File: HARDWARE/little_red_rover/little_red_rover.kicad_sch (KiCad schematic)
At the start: 60 parts, among them J1 USB_C_Receptacle_USB2.0_14P, J2 Conn_01x04_Socket, J3 Conn_01x02_Socket, J4 Conn_01x02_Socket, J5 Conn_01x01_Socket, J6 Conn_01x01_Socket, J8 Conn_02x12_Odd_Even, SW1 SW_Push, SW2 SW_Push, SW3 SW_Push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

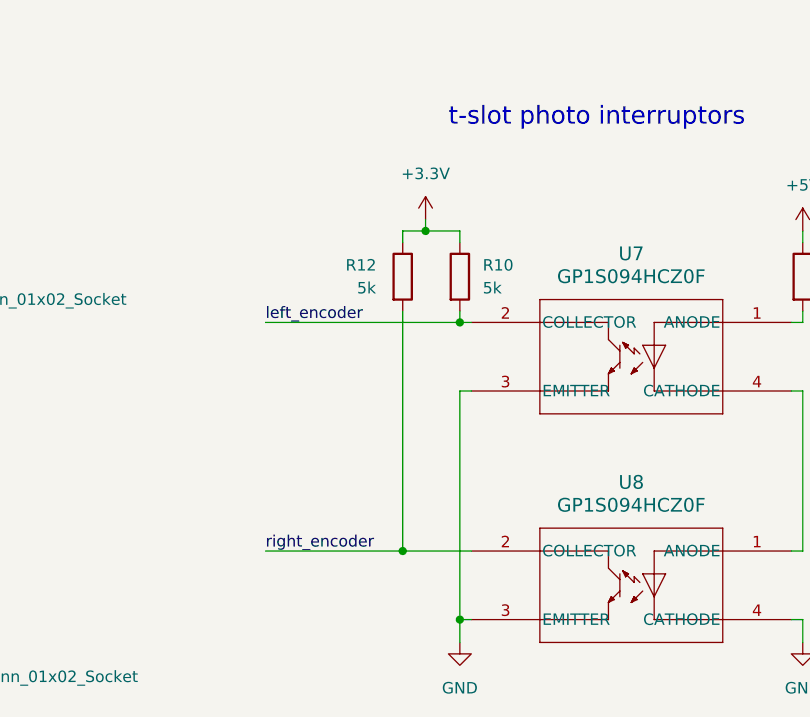
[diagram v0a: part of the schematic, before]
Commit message: Remove pull ups on photointerupters
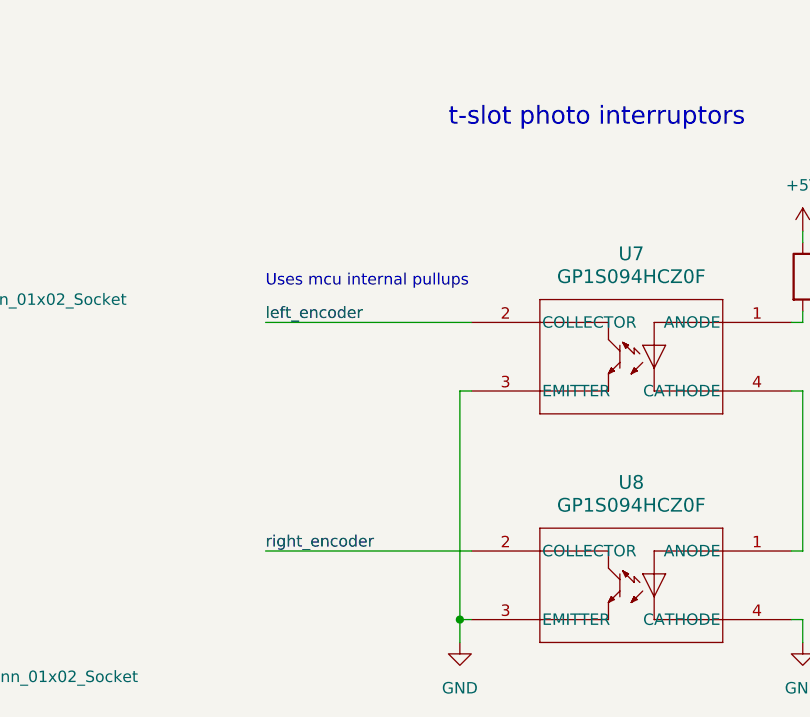
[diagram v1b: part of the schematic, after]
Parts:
- removed R10, R12: 5k, Resistor_SMD:R_0603_1608Metric_Pad0.98x0.95mm_HandSolder, symbol Device:R
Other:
- note added: "Uses mcu internal pullups"
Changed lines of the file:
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@@
   (junction (at 281.94 266.7) (diameter 0) (color 0 0 0 0)
   )
-  (junction (at 152.4 243.84) (diameter 0) (color 0 0 0 0)
-  )
   (junction (at 349.25 101.6) (diameter 0) (color 0 0 0 0)
   )
@@
   (junction (at 476.25 144.78) (diameter 0) (color 0 0 0 0)
   )
-  (junction (at 156.21 254) (diameter 0) (color 0 0 0 0)
-  )
   (junction (at 396.24 74.93) (diameter 0) (color 0 0 0 0)
   )
@@
   (junction (at 322.58 88.9) (diameter 0) (color 0 0 0 0)
   )
-  (junction (at 149.86 279.4) (diameter 0) (color 0 0 0 0)
-  )
   (junction (at 499.11 138.43) (diameter 0) (color 0 0 0 0)
   )
@@
     (stroke (width 0) (type default))
   )
-  (wire (pts (xy 149.86 279.4) (xy 157.48 279.4))
+  (wire (pts (xy 134.62 279.4) (xy 157.48 279.4))
     (stroke (width 0) (type default))
   )
@@
     (stroke (width 0) (type default))
   )
-  (wire (pts (xy 134.62 254) (xy 156.21 254))
-    (stroke (width 0) (type default))
-  )
   (wire (pts (xy 83.82 331.47) (xy 83.82 328.93))
     (stroke (width 0) (type default))
@@
     (stroke (width 0) (type default))
   )
-  (wire (pts (xy 149.86 245.11) (xy 149.86 243.84))
-    (stroke (width 0) (type default))
-  )
   (wire (pts (xy 46.99 73.66) (xy 67.31 73.66))
     (stroke (width 0) (type default))
@@
     (stroke (width 0) (type default))
   )
-  (wire (pts (xy 156.21 252.73) (xy 156.21 254))
-    (stroke (width 0) (type default))
-  )
   (wire (pts (xy 600.71 260.35) (xy 623.57 260.35))
     (stroke (width 0) (type default))
@@
     (stroke (width 0) (type default))
   )
-  (wire (pts (xy 152.4 242.57) (xy 152.4 243.84))
-    (stroke (width 0) (type default))
-  )
   (wire (pts (xy 57.15 342.9) (xy 68.58 342.9))
     (stroke (width 0) (type default))
@@
     (stroke (width 0) (type default))
   )
-  (wire (pts (xy 134.62 279.4) (xy 149.86 279.4))
-    (stroke (width 0) (type default))
-  )
   (wire (pts (xy 85.09 299.72) (xy 91.44 299.72))
     (stroke (width 0) (type default))
@@
     (stroke (width 0) (type default))
   )
-  (wire (pts (xy 149.86 252.73) (xy 149.86 279.4))
-    (stroke (width 0) (type default))
-  )
   (wire (pts (xy 392.43 158.75) (xy 392.43 161.29))
     (stroke (width 0) (type default))
@@
     (stroke (width 0) (type default))
   )
-  (wire (pts (xy 156.21 243.84) (xy 156.21 245.11))
-    (stroke (width 0) (type default))
-  )
   (wire (pts (xy 698.5 132.08) (xy 698.5 135.89))
     (stroke (width 0) (type default))
@@
     (stroke (width 0) (type default))
   )
-  (wire (pts (xy 156.21 243.84) (xy 152.4 243.84))
-    (stroke (width 0) (type default))
-  )
   (wire (pts (xy 322.58 73.66) (xy 328.93 73.66))
     (stroke (width 0) (type default))
@@
     (stroke (width 0) (type default))
   )
-  (wire (pts (xy 149.86 243.84) (xy 152.4 243.84))
-    (stroke (width 0) (type default))
-  )
   (wire (pts (xy 67.31 91.44) (xy 46.99 91.44))
     (stroke (width 0) (type default))
@@
     (stroke (width 0) (type default))
   )
-  (wire (pts (xy 156.21 254) (xy 157.48 254))
+  (wire (pts (xy 134.62 254) (xy 157.48 254))
     (stroke (width 0) (type default))
   )
@@
     (effects (font (size 5 5)) (justify left bottom))
   )
+  (text "Uses mcu internal pullups" (at 134.62 250.19 0)
+    (effects (font (size 1.27 1.27)) (justify left bottom))
+  )
   (text "headers" (at 628.65 35.56 0)
     (effects (font (size 5 5)) (justify left bottom))
@@
     )
   )
-  (symbol (lib_id "power:+3.3V") (at 152.4 242.57 0) (unit 1)
-    (in_bom yes) (on_board yes) (dnp no) (fields_autoplaced)
-    (property "Reference" "#PWR026" (at 152.4 246.38 0)
-      (effects (font (size 1.27 1.27)) hide)
-    )
-    (property "Value" "+3.3V" (at 152.4 237.49 0)
-      (effects (font (size 1.27 1.27)))
-    )
-    (property "Footprint" "" (at 152.4 242.57 0)
-      (effects (font (size 1.27 1.27)) hide)
-    )
-    (property "Datasheet" "" (at 152.4 242.57 0)
-      (effects (font (size 1.27 1.27)) hide)
-    )
-    (pin "1")
-    (instances
-      (project "little_red_rover"
-        (path "/6f482c50-19c8-43f6-b4b5-8739f6fb7866"
-          (reference "#PWR026") (unit 1)
-        )
-      )
-    )
-  )
   (symbol (lib_id "Device:R") (at 387.35 72.39 90) (unit 1)
     (in_bom yes) (on_board yes) (dnp no)
@@
     )
   )
-  (symbol (lib_id "Device:R") (at 149.86 248.92 0) (unit 1)
-    (in_bom yes) (on_board yes) (dnp no)
-    (property "Reference" "R12" (at 143.51 247.65 0)
-      (effects (font (size 1.27 1.27)) (justify left))
-    )
-    (property "Value" "5k" (at 144.78 250.19 0)
-      (effects (font (size 1.27 1.27)) (justify left))
-    )
-    (property "Footprint" "Resistor_SMD:R_0603_1608Metric_Pad0.98x0.95mm_HandSolder" (at 148.082 248.92 90)
-      (effects (font (size 1.27 1.27)) hide)
-    )
-    (property "Datasheet" "~" (at 149.86 248.92 0)
-      (effects (font (size 1.27 1.27)) hide)
-    )
-    (property "JLC" "0603" (at 149.86 248.92 0)
-      (effects (font (size 1.27 1.27)) hide)
-    )
-    (property "LCSC" "" (at 149.86 248.92 0)
-      (effects (font (size 1.27 1.27)) hide)
-    )
-    (pin "2")
-    (pin "1")
-    (instances
-      (project "little_red_rover"
-        (path "/6f482c50-19c8-43f6-b4b5-8739f6fb7866"
-          (reference "R12") (unit 1)
-        )
-      )
-    )
-  )
   (symbol (lib_id "power:GND") (at 623.57 280.67 0) (unit 1)
     (in_bom yes) (on_board yes) (dnp no) (fields_autoplaced)
@@
         )
       )
-    )
-  )
-  (symbol (lib_id "Device:R") (at 156.21 248.92 0) (unit 1)
-    (in_bom yes) (on_board yes) (dnp no) (fields_autoplaced)
-    (property "Reference" "R10" (at 158.75 247.65 0)
-      (effects (font (size 1.27 1.27)) (justify left))
-    )
-    (property "Value" "5k" (at 158.75 250.19 0)
-      (effects (font (size 1.27 1.27)) (justify left))
-    )
-    (property "Footprint" "Resistor_SMD:R_0603_1608Metric_Pad0.98x0.95mm_HandSolder" (at 154.432 248.92 90)
-      (effects (font (size 1.27 1.27)) hide)
-    )
-    (property "Datasheet" "~" (at 156.21 248.92 0)
-      (effects (font (size 1.27 1.27)) hide)
-    )
-    (property "JLC" "0603" (at 156.21 248.92 0)
-      (effects (font (size 1.27 1.27)) hide)
-    )
-    (property "LCSC" "" (at 156.21 248.92 0)
-      (effects (font (size 1.27 1.27)) hide)
-    )
-    (pin "2")
-    (pin "1")
-    (instances
-      (project "little_red_rover"
-        (path "/6f482c50-19c8-43f6-b4b5-8739f6fb7866"
-          (reference "R10") (unit 1)
-        )
-      )

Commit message: v1.1 ordered
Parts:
- C13, C14, C15, C6, R16, R17, R9: JLC (none) -> 0603
- J8: JLC (none) -> DNF
- SW1, SW2, SW3: JLC (none) -> -; LCSC (none) -> C2689642
- U10: JLC (none) -> SMD-41P; LCSC (none) -> C2913206
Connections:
- net usb_5v: now also U2.15 (TD)
- no-connect marks 7 -> 6
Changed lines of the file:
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@@
   (junction (at 77.47 342.9) (diameter 0) (color 0 0 0 0)
   )
+  (junction (at 346.71 57.15) (diameter 0) (color 0 0 0 0)
+  )
   (junction (at 281.94 266.7) (diameter 0) (color 0 0 0 0)
   )
@@
   (no_connect (at 284.48 269.24))
   (no_connect (at 314.96 266.7))
-  (no_connect (at 370.84 88.9))
   (no_connect (at 314.96 269.24))
   (wire (pts (xy 269.24 162.56) (xy 269.24 160.02))
@@
     (stroke (width 0) (type default))
   )
+  (wire (pts (xy 372.11 57.15) (xy 346.71 57.15))
+    (stroke (width 0) (type default))
+  )
   (wire (pts (xy 77.47 344.17) (xy 77.47 342.9))
     (stroke (width 0) (type default))
@@
     (stroke (width 0) (type default))
   )
+  (wire (pts (xy 370.84 88.9) (xy 372.11 88.9))
+    (stroke (width 0) (type default))
+  )
   (wire (pts (xy 74.93 234.95) (xy 74.93 236.22))
     (stroke (width 0) (type default))
@@
     (stroke (width 0) (type default))
   )
+  (wire (pts (xy 372.11 88.9) (xy 372.11 57.15))
+    (stroke (width 0) (type default))
+  )
   (wire (pts (xy 373.38 76.2) (xy 373.38 77.47))
     (stroke (width 0) (type default))
@@
       (effects (font (size 1.27 1.27)) hide)
     )
+    (property "JLC" "0603" (at 558.8 142.24 0)
+      (effects (font (size 1.27 1.27)) hide)
+    )
     (pin "2")
     (pin "1")
@@
       (effects (font (size 1.27 1.27)) hide)
     )
+    (property "JLC" "0603" (at 485.14 144.78 0)
+      (effects (font (size 1.27 1.27)) hide)
+    )
     (pin "2")
     (pin "1")
@@
       (effects (font (size 1.27 1.27)) hide)
     )
+    (property "JLC" "0603" (at 485.14 68.58 0)
+      (effects (font (size 1.27 1.27)) hide)
+    )
     (pin "2")
     (pin "1")
@@
   (symbol (lib_id "Power_Management:BQ24230RGT") (at 360.68 81.28 0) (unit 1)
     (in_bom yes) (on_board yes) (dnp no)
-    (property "Reference" "U2" (at 360.68 54.61 0)
+    (property "Reference" "U2" (at 360.68 50.8 0)
       (effects (font (size 1.27 1.27)))
     )
-    (property "Value" "BQ24230RGT" (at 360.68 58.42 0)
+    (property "Value" "BQ24230RGT" (at 360.68 54.61 0)
       (effects (font (size 1.27 1.27)))
     )
@@
       (effects (font (size 1.27 1.27)) hide)
     )
+    (property "JLC" "DNF" (at 690.88 116.84 0)
+      (effects (font (size 1.27 1.27)) hide)
+    )
     (pin "24")
     (pin "15")
@@
       (effects (font (size 1.27 1.27)) hide)
     )
+    (property "JLC" "0603" (at 485.14 83.82 0)
+      (effects (font (size 1.27 1.27)) hide)
+    )
     (pin "1")
     (pin "2")
@@
       (effects (font (size 1.27 1.27)) hide)
     )
+    (property "JLC" "-" (at 561.34 81.28 0)
+      (effects (font (size 1.27 1.27)) hide)
+    )
+    (property "LCSC" "C2689642" (at 561.34 81.28 0)
+      (effects (font (size 1.27 1.27)) hide)
+    )
     (pin "1")
     (pin "2")
@@
       (effects (font (size 1.27 1.27)) hide)
     )
+    (property "JLC" "0603" (at 561.34 68.58 0)
+      (effects (font (size 1.27 1.27)) hide)
+    )
     (pin "2")
     (pin "1")
@@
       (effects (font (size 1.27 1.27)) hide)
     )
+    (property "JLC" "0603" (at 499.11 130.81 0)
+      (effects (font (size 1.27 1.27)) hide)
+    )
     (pin "2")
     (pin "1")
@@
       (effects (font (size 1.27 1.27)) hide)
     )
+    (property "JLC" "SMD-41P" (at 113.03 109.22 0)
+      (effects (font (size 1.27 1.27)) hide)
+    )
+    (property "LCSC" "C2913206" (at 113.03 109.22 0)
+      (effects (font (size 1.27 1.27)) hide)
+    )
     (pin "22")
     (pin "63")
@@
       (effects (font (size 1.27 1.27)) hide)
     )
+    (property "JLC" "-" (at 485.14 138.43 0)
+      (effects (font (size 1.27 1.27)) hide)
+    )
+    (property "LCSC" "C2689642" (at 485.14 138.43 0)
+      (effects (font (size 1.27 1.27)) hide)
+    )
     (pin "1")
     (pin "2")
@@
       (effects (font (size 1.27 1.27)) hide)
     )
+    (property "JLC" "0603" (at 561.34 87.63 0)
+      (effects (font (size 1.27 1.27)) hide)
+    )
     (pin "2")
     (pin "1")
@@
       (effects (font (size 1.27 1.27)) hide)
     )
+    (property "JLC" "-" (at 561.34 62.23 0)
+      (effects (font (size 1.27 1.27)) hide)
+    )
+    (property "LCSC" "C2689642" (at 561.34 62.23 0)
+      (effects (font (size 1.27 1.27)) hide)
+    )

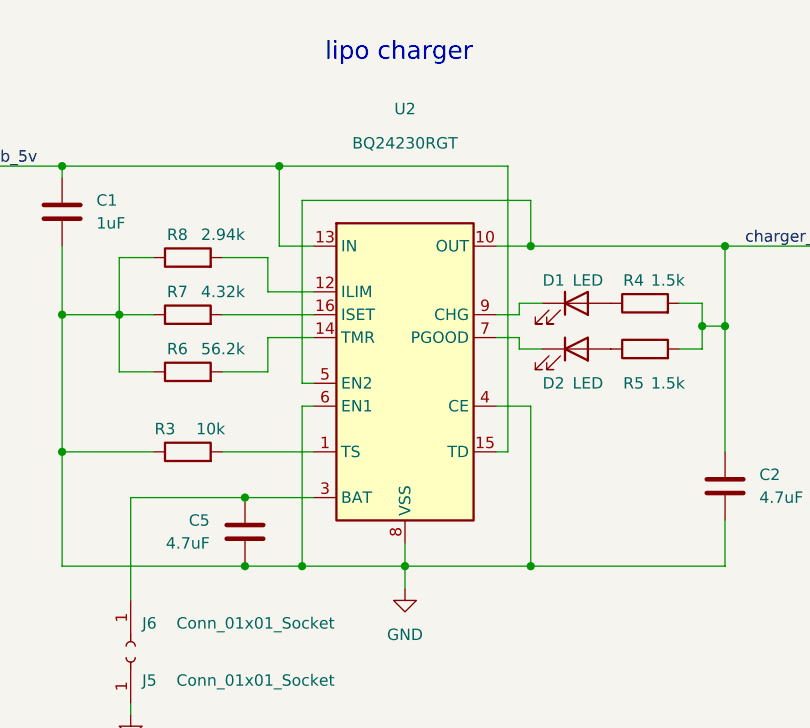
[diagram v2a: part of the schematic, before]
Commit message: Tie charger TD low to enable charge termination
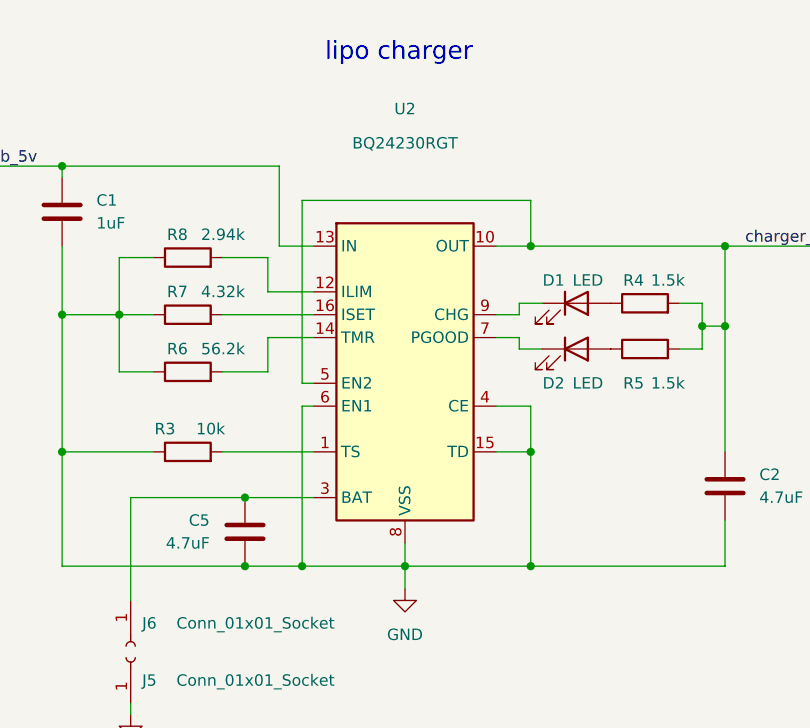
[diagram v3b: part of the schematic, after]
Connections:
- net GND: now also U2.15 (TD)
- net usb_5v: no longer U2.15 (TD)
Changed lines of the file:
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@@
   (junction (at 77.47 342.9) (diameter 0) (color 0 0 0 0)
   )
-  (junction (at 346.71 57.15) (diameter 0) (color 0 0 0 0)
-  )
   (junction (at 281.94 266.7) (diameter 0) (color 0 0 0 0)
   )
@@
   )
   (junction (at 570.23 81.28) (diameter 0) (color 0 0 0 0)
+  )
+  (junction (at 374.65 88.9) (diameter 0) (color 0 0 0 0)
   )
   (junction (at 256.54 105.41) (diameter 0) (color 0 0 0 0)
@@
     (stroke (width 0) (type default))
   )
-  (wire (pts (xy 374.65 101.6) (xy 360.68 101.6))
+  (wire (pts (xy 360.68 101.6) (xy 374.65 101.6))
     (stroke (width 0) (type default))
   )
@@
     (stroke (width 0) (type default))
   )
-  (wire (pts (xy 372.11 57.15) (xy 346.71 57.15))
-    (stroke (width 0) (type default))
-  )
   (wire (pts (xy 77.47 344.17) (xy 77.47 342.9))
     (stroke (width 0) (type default))
   )
+  (wire (pts (xy 374.65 88.9) (xy 374.65 101.6))
+    (stroke (width 0) (type default))
+  )
   (wire (pts (xy 364.49 163.83) (xy 386.08 163.83))
     (stroke (width 0) (type default))
@@
     (stroke (width 0) (type default))
   )
-  (wire (pts (xy 370.84 88.9) (xy 372.11 88.9))
+  (wire (pts (xy 370.84 88.9) (xy 374.65 88.9))
     (stroke (width 0) (type default))
   )
@@
     (stroke (width 0) (type default))
   )
-  (wire (pts (xy 374.65 83.82) (xy 374.65 101.6))
+  (wire (pts (xy 374.65 83.82) (xy 374.65 88.9))
     (stroke (width 0) (type default))
   )
@@
     (stroke (width 0) (type default))
   )
-  (wire (pts (xy 372.11 88.9) (xy 372.11 57.15))
-    (stroke (width 0) (type default))
-  )

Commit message: Added controller support
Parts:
- R14, R15: footprint Capacitor_SMD:C_0603_1608Metric_Pad1.08x0.95mm_HandSolder -> Resistor_SMD:R_0603_1608Metric_Pad0.98x0.95mm_HandSolder
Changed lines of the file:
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@@
       (effects (font (size 1.27 1.27)) (justify left))
     )
-    (property "Footprint" "Capacitor_SMD:C_0603_1608Metric_Pad1.08x0.95mm_HandSolder" (at 277.622 270.51 90)
+    (property "Footprint" "Resistor_SMD:R_0603_1608Metric_Pad0.98x0.95mm_HandSolder" (at 277.622 270.51 90)
       (effects (font (size 1.27 1.27)) hide)
     )
@@
       (effects (font (size 1.27 1.27)) (justify left))
     )
-    (property "Footprint" "Capacitor_SMD:C_0603_1608Metric_Pad1.08x0.95mm_HandSolder" (at 270.002 270.51 90)
-      (effects (font (size 1.27 1.27)) hide)
-    )
+    (property "Footprint" "Resistor_SMD:R_0603_1608Metric_Pad0.98x0.95mm_HandSolder" (at 270.002 270.51 90)
+      (effects (font (size 1.27 1.27)) hide)
+    )

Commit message: Update schematic: reverse polarity protection, JST motor connectors, power switch
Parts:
- removed D1, D2: LED, LED_SMD:LED_0603_1608Metric_Pad1.05x0.95mm_HandSolder, symbol Device:LED
- removed J3, J4: Conn_01x02_Socket, Connector_PinSocket_2.54mm:PinSocket_1x02_P2.54mm_Horizontal, symbol Connector:Conn_01x02_Socket
- removed R7: 4.32k, Resistor_SMD:R_0603_1608Metric_Pad0.98x0.95mm_HandSolder, symbol Device:R
- removed R8: 2.94k, Resistor_SMD:R_0603_1608Metric_Pad0.98x0.95mm_HandSolder, symbol Device:R
- removed U7, U8: GP1S094HCZ0F, digikey_imports:TO_4HCZ0F_SHP, symbol digikey_imports:GP1S094HCZ0F
- added D7, D8: LED, LED_SMD:LED_0603_1608Metric_Pad1.05x0.95mm_HandSolder, symbol Device:LED
- added J7, J9: Conn_01x06, Connector_JST:JST_PH_B6B-PH-K_1x06_P2.00mm_Vertical, symbol Connector_Generic:Conn_01x06
- added Q1, Q2: PMOS, Package_TO_SOT_SMD:SOT-23_Handsoldering, symbol Simulation_SPICE:PMOS
- added R10: 47k, Resistor_SMD:R_0603_1608Metric_Pad0.98x0.95mm_HandSolder, symbol Device:R
- added R12, R18: 1.5k, Resistor_SMD:R_0603_1608Metric_Pad0.98x0.95mm_HandSolder, symbol Device:R
- added R19: 56.2k, Resistor_SMD:R_0603_1608Metric_Pad0.98x0.95mm_HandSolder, symbol Device:R
- added SW4: SW_DIP_x01, Button_Switch_SMD:SW_SPDT_PCM12, symbol Switch:SW_DIP_x01
- R11: value 560 -> 47k
- R4: value 1.5k -> 2.94k
- R5: value 1.5k -> 4.32k
- R6: value 56.2k -> 47k
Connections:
- net +3.3V: now also J7.4 (Pin_4), J9.4 (Pin_4)
- net +5V: no longer R11.1
- net GND: now also J8.1 (Pin_1), J8.2 (Pin_2), J8.4 (Pin_4), R3.2, R4.2, R5.2, J7.1 (Pin_1), J9.1 (Pin_1), R10.1, R19.2; no longer R3.1
- net charger_out: now also Q1.1 (D), R12.2, R18.2; no longer C4.1, L2.1, R4.2, R5.2, U3.1 (VIN), U3.3 (EN)
- net at R11.2: now also Q1.2 (G)
- net ILIM: now reaches R4.1
- net ILIM: now also U2.12 (ILIM)
- net PGOOD: now reaches U2.7 (PGOOD)
- net PGOOD: now also D8.1 (K)
- net ISET: now reaches R5.1
- net ISET: now also U2.16 (ISET)
- net CHG: now reaches U2.9 (CHG)
- net CHG: now also D7.1 (K)
- net +BATT: now reaches C5.1, U2.2 (BAT), U2.3 (BAT)
- net +BATT: now also Q2.3 (S), SW4.2; no longer J6.1 (Pin_1)
- net TS: now reaches U2.1 (TS)
- net TS: now also R3.1; no longer R3.2
- net at R6.2: now also Q2.2 (G); no longer U2.14 (TMR)
- net right_motor_+: now reaches U6.2 (OUT1)
- net right_motor_+: now also J9.5 (Pin_5)
- net right_motor_-: now reaches U6.3 (OUT2)
- net right_motor_-: now also J9.6 (Pin_6)
- net left_motor_+: now reaches U5.2 (OUT1)
- net left_motor_+: now also J7.5 (Pin_5)
- net left_motor_-: now reaches U5.3 (OUT2)
- net left_motor_-: now also J7.6 (Pin_6)
- net GPIO_12 renamed lidar_enable
- net lidar_enable: no longer J8.2 (Pin_2)
- net GPIO_13 renamed left_encoder_a
- net left_encoder_a: now also J7.2 (Pin_2); no longer J8.1 (Pin_1)
- net GPIO_14 renamed left_encoder_b
- net left_encoder_b: now also J7.3 (Pin_3); no longer J8.4 (Pin_4)
- net left_encoder renamed right_encoder_b
- net right_encoder_b: now also J9.3 (Pin_3)
- net right_encoder renamed right_encoder_a
- net right_encoder_a: now also J9.2 (Pin_2)
- new net: D8.2 (A), R18.1
- new net: R10.2, R11.1, SW4.1
- new net: D7.2 (A), R12.1
- new net TMR: R19.1, U2.14 (TMR)
- new net VDD: C4.1, L2.1, Q1.3 (S), U3.1 (VIN), U3.3 (EN)
- new net bat_+: J6.1 (Pin_1), Q2.1 (D)
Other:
- note added: "Motor connectors"
- note added: "battery connector"
- note added: "power switch"
- note added: "reverse polarity protection"
- note removed: "Uses mcu internal pullups"
- note removed: "t-slot photo interruptors"
- moved on the sheet: C1, C10, C11, C12, C13, C14, C15, C2, C3, C4, C5, C6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
